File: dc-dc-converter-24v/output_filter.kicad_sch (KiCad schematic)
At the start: 3 parts

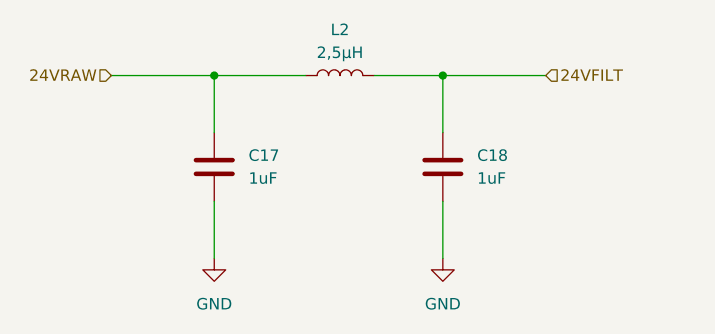
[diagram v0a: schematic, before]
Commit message: improve output filter of DC-DC converter
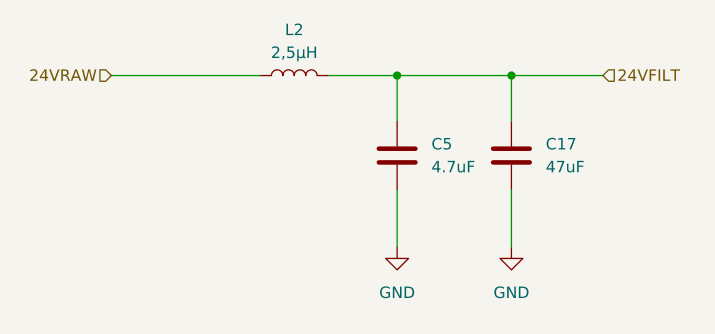
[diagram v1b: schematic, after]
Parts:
- removed C17, C18: 1uF, benediktibk:C_0603_1608Metric_Pad1.08x0.95mm_HandSolder, symbol benediktibk:C_1uF_SMD_0603_50V_10%
- added C17: 47uF, benediktibk:C_1206_3216Metric_Pad1.33x1.80mm_HandSolder, symbol benediktibk:C_47uF_SMD_1206_25V_20%
- added C5: 4.7uF, benediktibk:C_0805_2012Metric_Pad1.18x1.45mm_HandSolder, symbol benediktibk:C_4_7uF_SMD_0805_50V_10%
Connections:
- net 24VFILT: now also C17.1, C5.1
- net GND: now also C17.2, C5.2
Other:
- moved on the sheet: L2
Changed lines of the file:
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@@
 (kicad_sch (version 20230121) (generator eeschema)
   (paper "A4")
-  (junction (at 123.19 46.99) (diameter 0) (color 0 0 0 0)
+  (junction (at 118.11 46.99) (diameter 0) (color 0 0 0 0)
   )
-  (junction (at 97.79 46.99) (diameter 0) (color 0 0 0 0)
+  (junction (at 130.81 46.99) (diameter 0) (color 0 0 0 0)
   )
-  (wire (pts (xy 115.57 46.99) (xy 123.19 46.99))
+  (wire (pts (xy 130.81 46.99) (xy 130.81 52.07))
     (stroke (width 0) (type default))
   )
-  (wire (pts (xy 97.79 60.96) (xy 97.79 67.31))
+  (wire (pts (xy 118.11 46.99) (xy 130.81 46.99))
     (stroke (width 0) (type default))
   )
-  (wire (pts (xy 97.79 46.99) (xy 107.95 46.99))
+  (wire (pts (xy 110.49 46.99) (xy 118.11 46.99))
     (stroke (width 0) (type default))
   )
-  (wire (pts (xy 123.19 46.99) (xy 134.62 46.99))
+  (wire (pts (xy 86.36 46.99) (xy 102.87 46.99))
     (stroke (width 0) (type default))
   )
-  (wire (pts (xy 123.19 46.99) (xy 123.19 53.34))
+  (wire (pts (xy 118.11 59.69) (xy 118.11 66.04))
     (stroke (width 0) (type default))
   )
-  (wire (pts (xy 86.36 46.99) (xy 97.79 46.99))
+  (wire (pts (xy 130.81 46.99) (xy 140.97 46.99))
     (stroke (width 0) (type default))
   )
-  (wire (pts (xy 97.79 46.99) (xy 97.79 53.34))
+  (wire (pts (xy 130.81 59.69) (xy 130.81 66.04))
     (stroke (width 0) (type default))
   )
-  (wire (pts (xy 123.19 60.96) (xy 123.19 67.31))
+  (wire (pts (xy 118.11 46.99) (xy 118.11 52.07))
     (stroke (width 0) (type default))
   )
-  (hierarchical_label "24VFILT" (shape input) (at 134.62 46.99 0) (fields_autoplaced)
+  (hierarchical_label "24VFILT" (shape input) (at 140.97 46.99 0) (fields_autoplaced)
     (effects (font (size 1.27 1.27)) (justify left))
   )
@@
     (effects (font (size 1.27 1.27)) (justify right))
   )
-  (symbol (lib_id "benediktibk:C_1uF_SMD_0603_50V_10%") (at 97.79 57.15 0) (unit 1)
+  (symbol (lib_id "benediktibk:L_2_5µH_30A") (at 106.68 46.99 90) (unit 1)
     (in_bom yes) (on_board yes) (dnp no) (fields_autoplaced)
-    (property "Reference" "C17" (at 101.6 55.88 0)
-      (effects (font (size 1.27 1.27)) (justify left))
+    (property "Reference" "L2" (at 106.68 41.91 90)
+      (effects (font (size 1.27 1.27)))
     )
-    (property "Value" "1uF" (at 101.6 58.42 0)
-      (effects (font (size 1.27 1.27)) (justify left))
+    (property "Value" "2,5µH" (at 106.68 44.45 90)
+      (effects (font (size 1.27 1.27)))
     )
-    (property "Footprint" "benediktibk:C_0603_1608Metric_Pad1.08x0.95mm_HandSolder" (at 98.7552 60.96 0)
+    (property "Footprint" "" (at 106.68 46.99 0)
       (effects (font (size 1.27 1.27)) hide)
     )
-    (property "Datasheet" "~" (at 97.79 57.15 0)
+    (property "Datasheet" "~" (at 106.68 46.99 0)
       (effects (font (size 1.27 1.27)) hide)
     )
-    (property "RS order number" "103-4112" (at 115.316 55.88 0)
-      (effects (font (size 1.27 1.27)) hide)
-    )
-    (pin "1")
-    (pin "2")
-    (instances
-      (project "dc-dc-converter-24v"
-        (path "/f3858519-f688-4645-91dc-9843c9d0ed53/8f8f2bb4-fdfe-4421-bc8c-e8dc6b7f806e"
-          (reference "C17") (unit 1)
-        )
-      )
-    )
-  )
-  (symbol (lib_id "power:GND") (at 123.19 67.31 0) (unit 1)
-    (in_bom yes) (on_board yes) (dnp no) (fields_autoplaced)
-    (property "Reference" "#PWR025" (at 123.19 73.66 0)
-      (effects (font (size 1.27 1.27)) hide)
-    )
-    (property "Value" "GND" (at 123.19 72.39 0)
-      (effects (font (size 1.27 1.27)))
-    )
-    (property "Footprint" "" (at 123.19 67.31 0)
-      (effects (font (size 1.27 1.27)) hide)
-    )
-    (property "Datasheet" "" (at 123.19 67.31 0)
-      (effects (font (size 1.27 1.27)) hide)
-    )
-    (pin "1")
-    (instances
-      (project "dc-dc-converter-24v"
-        (path "/f3858519-f688-4645-91dc-9843c9d0ed53/8f8f2bb4-fdfe-4421-bc8c-e8dc6b7f806e"
-          (reference "#PWR025") (unit 1)
-        )
-      )
-    )
-  )
-  (symbol (lib_id "benediktibk:C_1uF_SMD_0603_50V_10%") (at 123.19 57.15 0) (unit 1)
-    (in_bom yes) (on_board yes) (dnp no) (fields_autoplaced)
-    (property "Reference" "C18" (at 127 55.88 0)
-      (effects (font (size 1.27 1.27)) (justify left))
-    )
-    (property "Value" "1uF" (at 127 58.42 0)
-      (effects (font (size 1.27 1.27)) (justify left))
-    )
-    (property "Footprint" "benediktibk:C_0603_1608Metric_Pad1.08x0.95mm_HandSolder" (at 124.1552 60.96 0)
-      (effects (font (size 1.27 1.27)) hide)
-    )
-    (property "Datasheet" "~" (at 123.19 57.15 0)
-      (effects (font (size 1.27 1.27)) hide)
-    )
-    (property "RS order number" "103-4112" (at 140.716 55.88 0)
-      (effects (font (size 1.27 1.27)) hide)
-    )
-    (pin "1")
-    (pin "2")
-    (instances
-      (project "dc-dc-converter-24v"
-        (path "/f3858519-f688-4645-91dc-9843c9d0ed53/8f8f2bb4-fdfe-4421-bc8c-e8dc6b7f806e"
-          (reference "C18") (unit 1)
-        )
-      )
-    )
-  )
-  (symbol (lib_id "benediktibk:L_2_5µH_30A") (at 111.76 46.99 90) (unit 1)
-    (in_bom yes) (on_board yes) (dnp no) (fields_autoplaced)
-    (property "Reference" "L2" (at 111.76 41.91 90)
-      (effects (font (size 1.27 1.27)))
-    )
-    (property "Value" "2,5µH" (at 111.76 44.45 90)
-      (effects (font (size 1.27 1.27)))
-    )
-    (property "Footprint" "" (at 111.76 46.99 0)
-      (effects (font (size 1.27 1.27)) hide)
-    )
-    (property "Datasheet" "~" (at 111.76 46.99 0)
-      (effects (font (size 1.27 1.27)) hide)
-    )
-    (property "RS order number" " 238-3683" (at 111.76 46.99 0)
+    (property "RS order number" " 238-3683" (at 106.68 46.99 0)
       (effects (font (size 1.27 1.27)) hide)
     )
@@
     )
   )
-  (symbol (lib_id "power:GND") (at 97.79 67.31 0) (unit 1)
+  (symbol (lib_id "power:GND") (at 118.11 66.04 0) (unit 1)
     (in_bom yes) (on_board yes) (dnp no) (fields_autoplaced)
-    (property "Reference" "#PWR024" (at 97.79 73.66 0)
+    (property "Reference" "#PWR05" (at 118.11 72.39 0)
       (effects (font (size 1.27 1.27)) hide)
     )
-    (property "Value" "GND" (at 97.79 72.39 0)
+    (property "Value" "GND" (at 118.11 71.12 0)
       (effects (font (size 1.27 1.27)))
     )
-    (property "Footprint" "" (at 97.79 67.31 0)
+    (property "Footprint" "" (at 118.11 66.04 0)
       (effects (font (size 1.27 1.27)) hide)
     )
-    (property "Datasheet" "" (at 97.79 67.31 0)
+    (property "Datasheet" "" (at 118.11 66.04 0)
       (effects (font (size 1.27 1.27)) hide)
     )
+    (pin "1")
+    (instances
+      (project "dc-dc-converter-24v"
+        (path "/f3858519-f688-4645-91dc-9843c9d0ed53/8f8f2bb4-fdfe-4421-bc8c-e8dc6b7f806e"
+          (reference "#PWR05") (unit 1)
+        )
+      )
+    )
+  )
+  (symbol (lib_id "benediktibk:C_4_7uF_SMD_0805_50V_10%") (at 118.11 55.88 0) (unit 1)
+    (in_bom yes) (on_board yes) (dnp no) (fields_autoplaced)
+    (property "Reference" "C5" (at 121.92 54.61 0)
+      (effects (font (size 1.27 1.27)) (justify left))
+    )
+    (property "Value" "4.7uF" (at 121.92 57.15 0)
+      (effects (font (size 1.27 1.27)) (justify left))
+    )
+    (property "Footprint" "benediktibk:C_0805_2012Metric_Pad1.18x1.45mm_HandSolder" (at 119.0752 59.69 0)
+      (effects (font (size 1.27 1.27)) hide)
+    )
+    (property "Datasheet" "~" (at 118.11 55.88 0)
+      (effects (font (size 1.27 1.27)) hide)
+    )
+    (property "RS order number" "113-8707" (at 135.636 54.61 0)
+      (effects (font (size 1.27 1.27)) hide)
+    )
+    (pin "1")
+    (pin "2")
+    (instances
+      (project "dc-dc-converter-24v"
+        (path "/f3858519-f688-4645-91dc-9843c9d0ed53/8f8f2bb4-fdfe-4421-bc8c-e8dc6b7f806e"
+          (reference "C5") (unit 1)
+        )
+      )
+    )
+  )
+  (symbol (lib_id "benediktibk:C_47uF_SMD_1206_25V_20%") (at 130.81 55.88 0) (unit 1)
+    (in_bom yes) (on_board yes) (dnp no) (fields_autoplaced)
+    (property "Reference" "C17" (at 134.62 54.61 0)
+      (effects (font (size 1.27 1.27)) (justify left))
+    )
+    (property "Value" "47uF" (at 134.62 57.15 0)
+      (effects (font (size 1.27 1.27)) (justify left))
+    )
+    (property "Footprint" "benediktibk:C_1206_3216Metric_Pad1.33x1.80mm_HandSolder" (at 131.7752 59.69 0)
+      (effects (font (size 1.27 1.27)) hide)
+    )
+    (property "Datasheet" "~" (at 130.81 55.88 0)
+      (effects (font (size 1.27 1.27)) hide)
+    )
+    (property "RS order number" "788-3060" (at 148.336 54.61 0)
+      (effects (font (size 1.27 1.27)) hide)
+    )
+    (pin "2")
+    (pin "1")
+    (instances
+      (project "dc-dc-converter-24v"
+        (path "/f3858519-f688-4645-91dc-9843c9d0ed53/8f8f2bb4-fdfe-4421-bc8c-e8dc6b7f806e"
+          (reference "C17") (unit 1)
+        )
+      )
+    )
+  )
+  (symbol (lib_id "power:GND") (at 130.81 66.04 0) (unit 1)
+    (in_bom yes) (on_board yes) (dnp no) (fields_autoplaced)
+    (property "Reference" "#PWR024" (at 130.81 72.39 0)
+      (effects (font (size 1.27 1.27)) hide)
+    )
+    (property "Value" "GND" (at 130.81 71.12 0)
+      (effects (font (size 1.27 1.27)))
+    )
+    (property "Footprint" "" (at 130.81 66.04 0)
+      (effects (font (size 1.27 1.27)) hide)
+    )
+    (property "Datasheet" "" (at 130.81 66.04 0)
+      (effects (font (size 1.27 1.27)) hide)
+    )

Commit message: update symbols and footprints
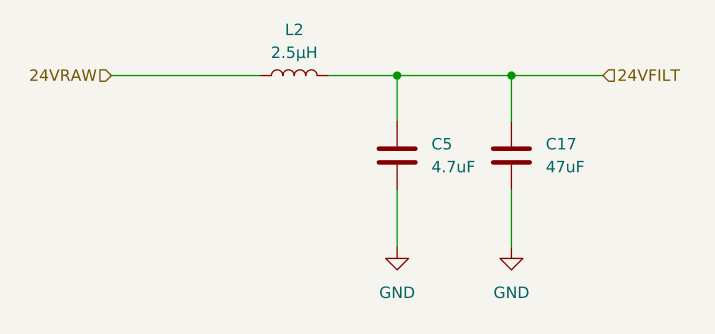
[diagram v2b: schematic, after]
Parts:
- L2: value 2,5µH -> 2.5µH; footprint (none) -> benediktibk:ETQP8
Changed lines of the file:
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@@
       (effects (font (size 1.27 1.27)))
     )
-    (property "Value" "2,5µH" (at 106.68 44.45 90)
+    (property "Value" "2.5µH" (at 106.68 44.45 90)
       (effects (font (size 1.27 1.27)))
     )
-    (property "Footprint" "" (at 106.68 46.99 0)
+    (property "Footprint" "benediktibk:ETQP8" (at 106.68 46.99 0)
       (effects (font (size 1.27 1.27)) hide)
     )
